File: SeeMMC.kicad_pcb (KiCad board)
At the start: 2 copper layers, 24 x 32 mm, 17 parts, among them J1 SD_Card, U1 TXS02612RTWR, U2 TPS7A1118PDRV

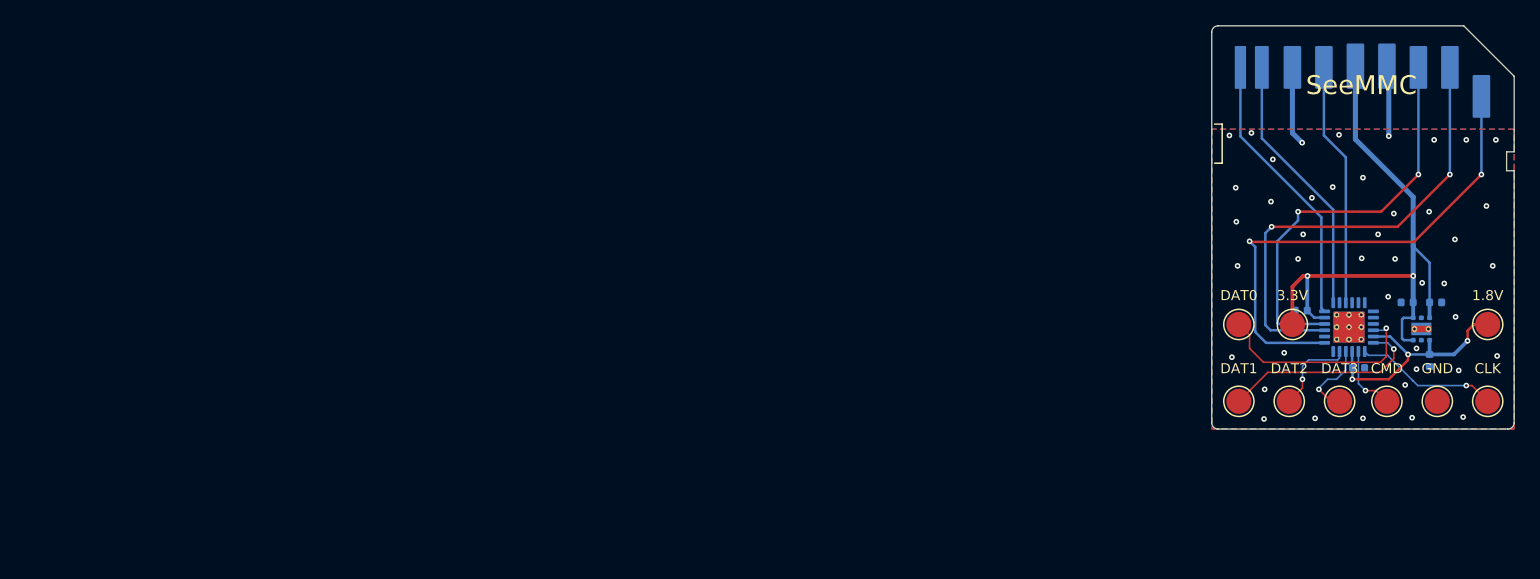
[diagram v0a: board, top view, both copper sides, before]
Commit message: Updated KiCad version
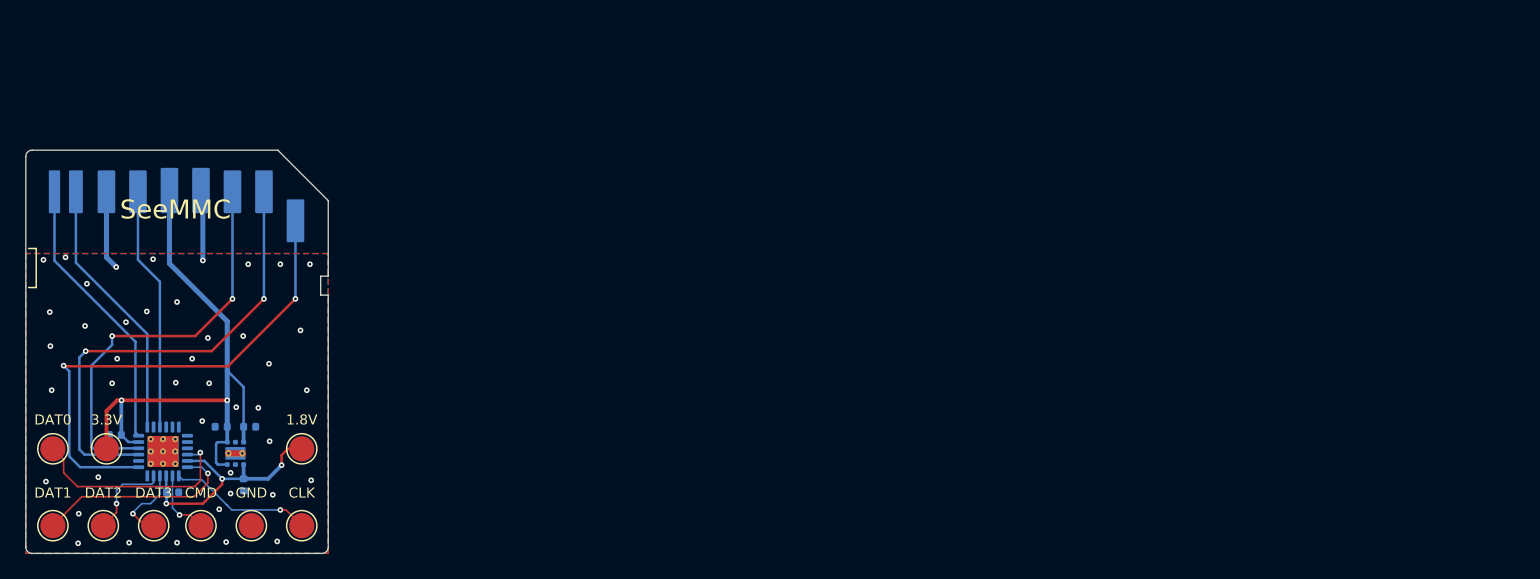
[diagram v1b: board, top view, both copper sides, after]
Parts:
- moved U2 94.6 mm to (70.6, 97.2)
- moved C4 94.6 mm to (71.7, 95.1)
- moved J1 94.6 mm to (66.0, 89.2)
- moved TP1 94.6 mm to (56.1, 96.9)
- moved TP2 94.6 mm to (56.1, 103.0)
- moved TP3 94.6 mm to (60.1, 103.0)
- moved TP4 94.6 mm to (64.1, 103.0)
- moved TP5 94.6 mm to (67.9, 103.0)
- moved TP6 94.6 mm to (60.4, 96.9)
- moved TP7 94.6 mm to (75.9, 103.0)
- moved TP8 94.6 mm to (71.9, 103.0)
- moved TP9 94.6 mm to (75.9, 96.9)
- moved U1 94.6 mm to (64.9, 97.1)
- moved C1 94.6 mm to (65.6, 100.3)
- moved C6 94.6 mm to (69.5, 95.1)
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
